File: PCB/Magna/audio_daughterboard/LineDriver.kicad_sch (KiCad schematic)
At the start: 27 parts, among them J101 PSG01550, Q101 NMOS, Q102 NMOS, U101 NE5532

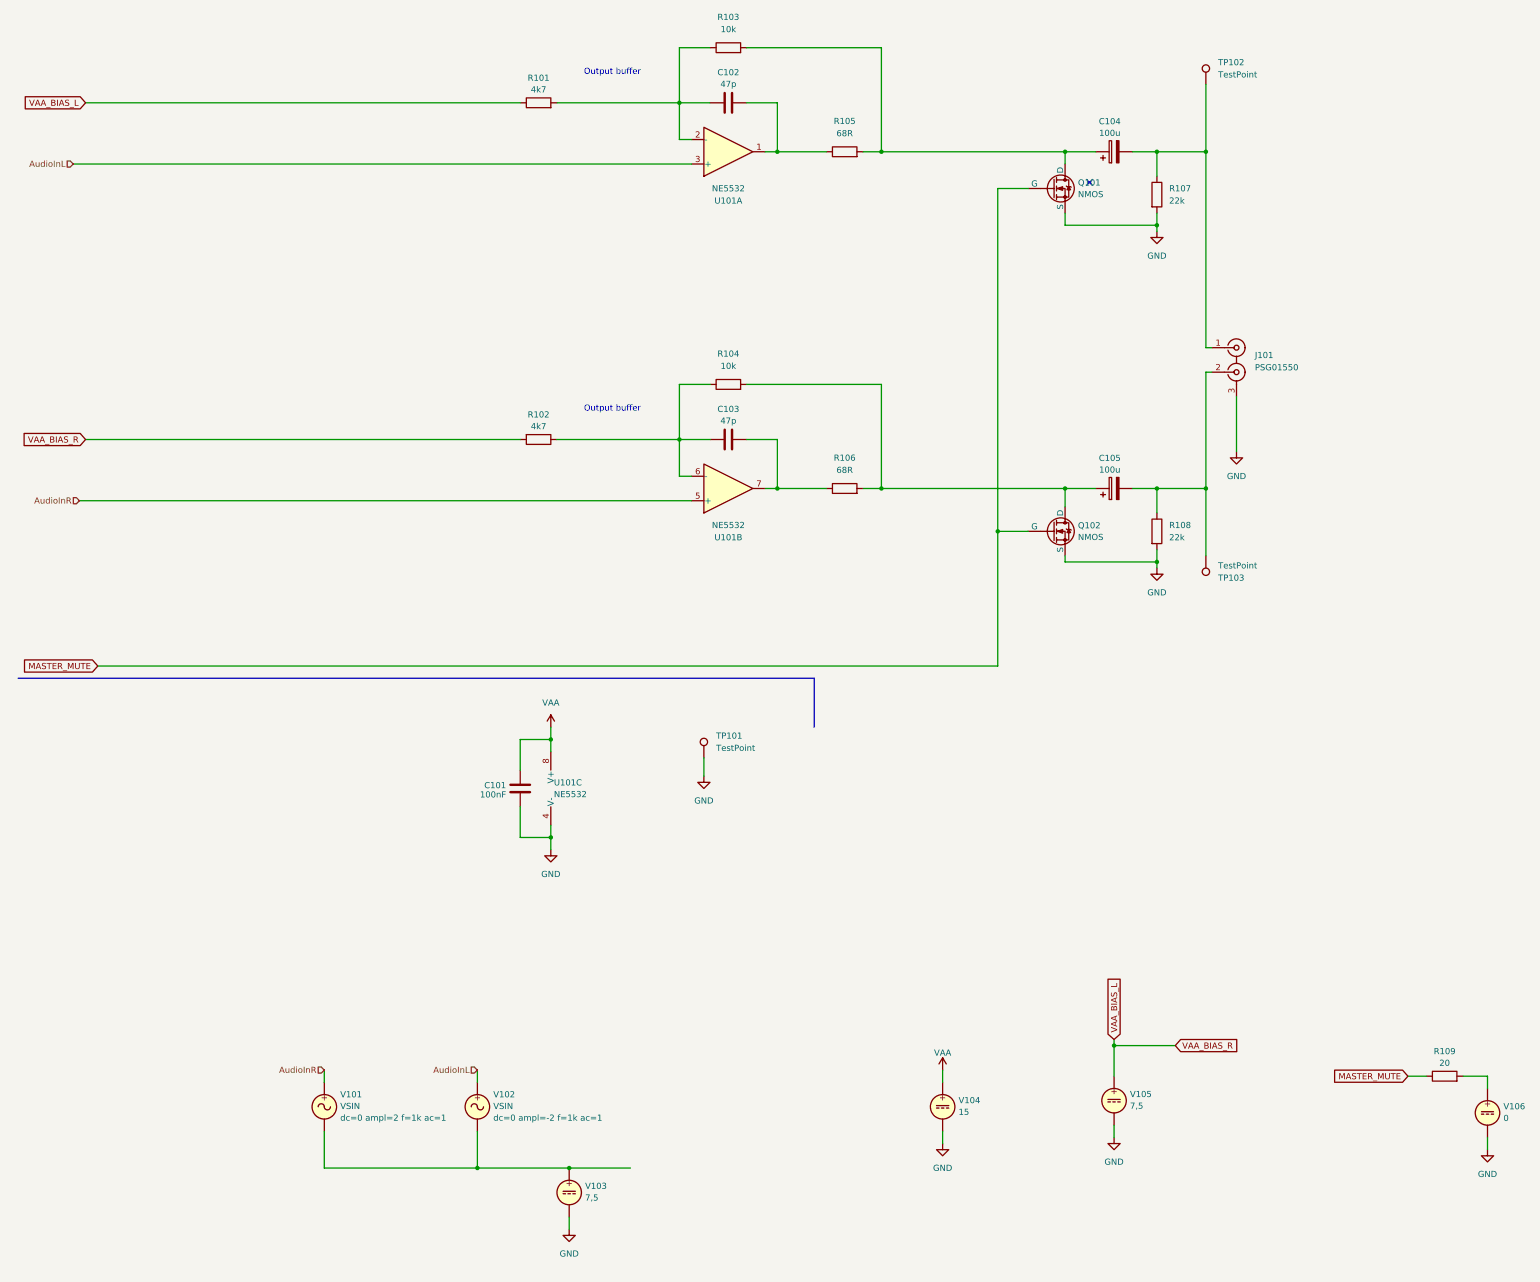
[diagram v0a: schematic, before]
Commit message: "Finalize" Audio daugherboard
Finished DAC output filter
Fixed the whole damn MCU subschematic
Fixed Linedriver schematic
Added component footprints and LCSC numbers
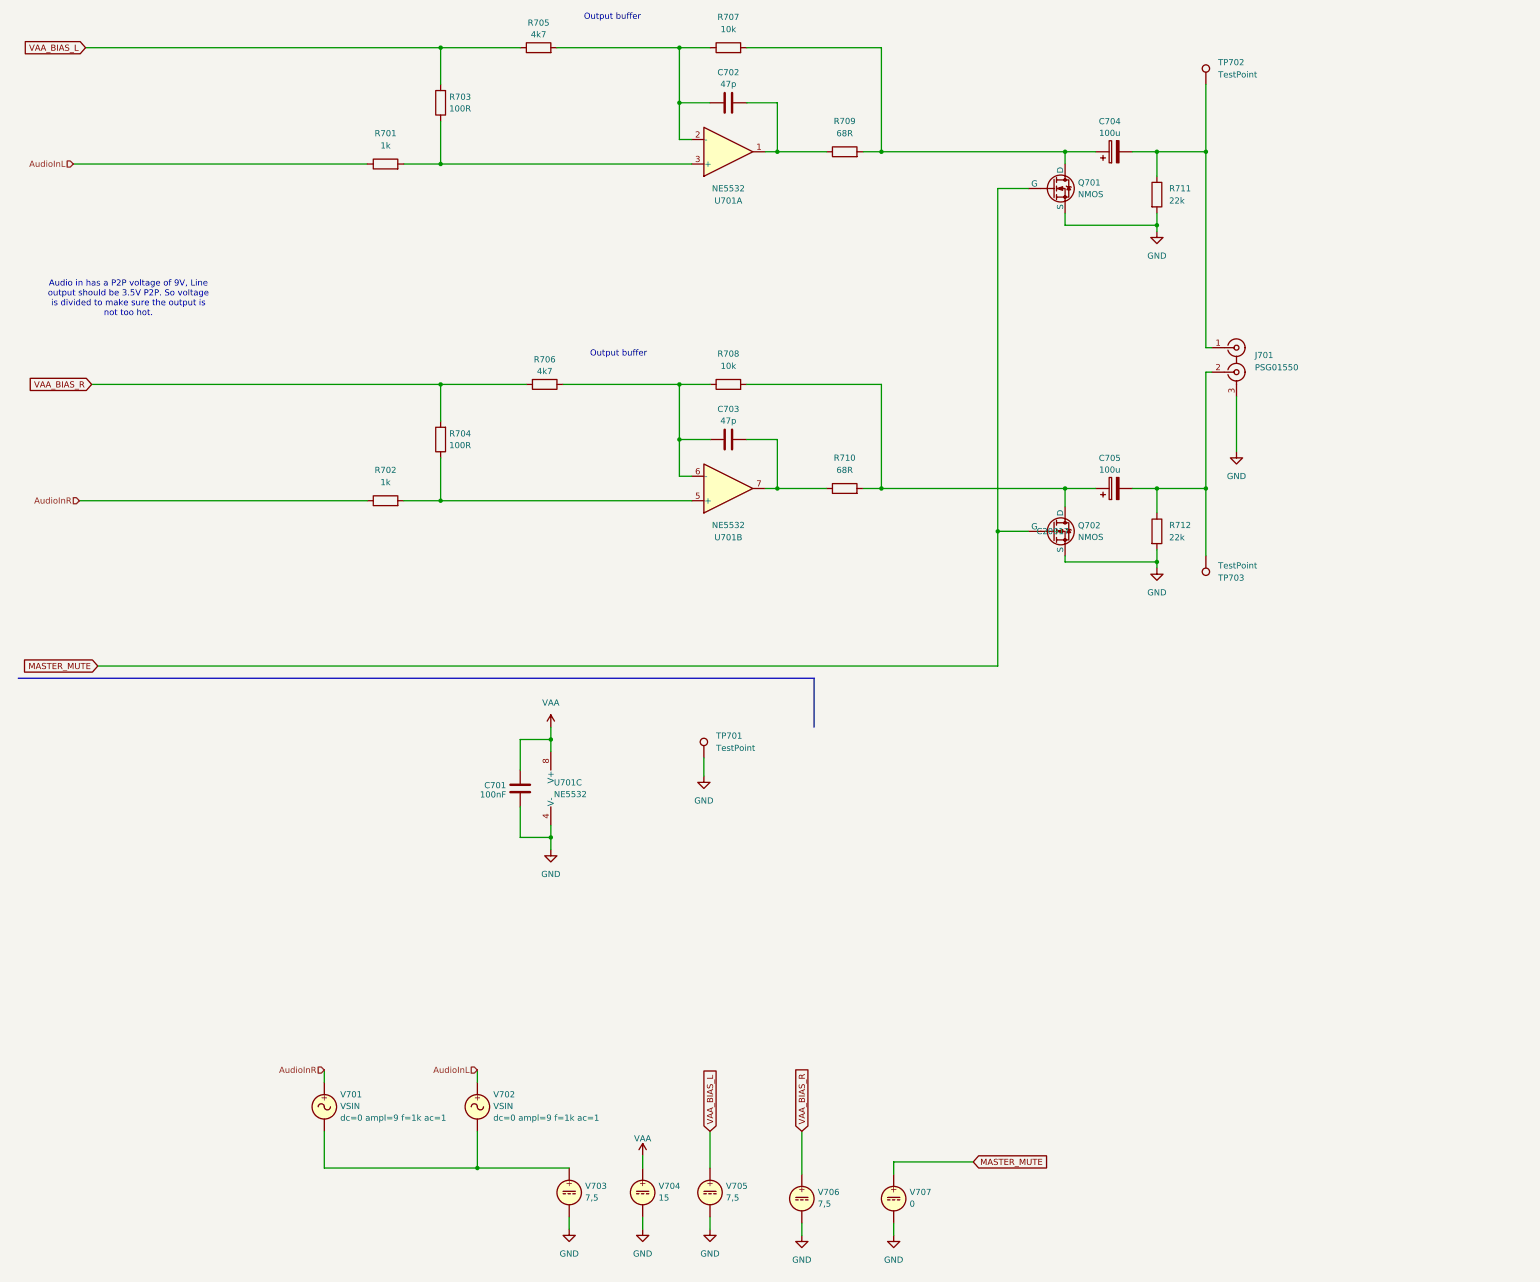
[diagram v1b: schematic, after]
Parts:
- removed C105: 100u, Capacitor_SMD:CP_Elec_6.3x5.8, symbol Device:C_Polarized
- removed R109: 20, Resistor_SMD:R_0805_2012Metric_Pad1.20x1.40mm_HandSolder, symbol Device:R
- added C705: 100u, Capacitor_SMD:CP_Elec_6.3x5.8, symbol Device:C_Polarized
- added R701, R702: 1k, Resistor_SMD:R_0603_1608Metric, symbol Device:R
- added R703, R704: 100R, Resistor_SMD:R_0603_1608Metric, symbol Device:R
- added V706: 7,5, symbol Simulation_SPICE:VDC
- C701: renamed from C101; now left out of the parts list
- C702: renamed from C102; now left out of the parts list
- C703: renamed from C103; now left out of the parts list
- C704: renamed from C104; now left out of the parts list
- J701: renamed from J101; now left out of the parts list
- Q701: renamed from Q101; footprint (none) -> Package_TO_SOT_SMD:SOT-23-3; LCSC (none) -> C20917; now left out of the parts list
- Q702: renamed from Q102; footprint (none) -> Package_TO_SOT_SMD:SOT-23-3; LCSC (none) -> C20917; now left out of the parts list
- R705: renamed from R101; footprint Resistor_SMD:R_0805_2012Metric_Pad1.20x1.40mm_HandSolder -> Resistor_SMD:R_0603_1608Metric; LCSC (none) -> C2989582; now left out of the parts list
- R706: renamed from R102; footprint Resistor_SMD:R_0805_2012Metric_Pad1.20x1.40mm_HandSolder -> Resistor_SMD:R_0603_1608Metric; LCSC (none) -> C2989582; now left out of the parts list
- R707: renamed from R103; footprint Resistor_SMD:R_0805_2012Metric_Pad1.20x1.40mm_HandSolder -> Resistor_SMD:R_0603_1608Metric; LCSC (none) -> C95204; now left out of the parts list
- R708: renamed from R104; footprint Resistor_SMD:R_0805_2012Metric_Pad1.20x1.40mm_HandSolder -> Resistor_SMD:R_0603_1608Metric; LCSC (none) -> C95204; now left out of the parts list
- R709: renamed from R105; footprint Resistor_SMD:R_0805_2012Metric_Pad1.20x1.40mm_HandSolder -> Resistor_SMD:R_0603_1608Metric; LCSC C865616 -> C351632; now left out of the parts list
- R710: renamed from R106; footprint Resistor_SMD:R_0805_2012Metric_Pad1.20x1.40mm_HandSolder -> Resistor_SMD:R_0603_1608Metric; LCSC C865616 -> C351632; now left out of the parts list
- R711: renamed from R107; footprint Resistor_SMD:R_0805_2012Metric_Pad1.20x1.40mm_HandSolder -> Resistor_SMD:R_0603_1608Metric; LCSC C479095 -> C335085; now left out of the parts list
- R712: renamed from R108; footprint Resistor_SMD:R_0805_2012Metric_Pad1.20x1.40mm_HandSolder -> Resistor_SMD:R_0603_1608Metric; LCSC C479095 -> C335085; now left out of the parts list
- TP701: renamed from TP101; now left out of the parts list
- TP702: renamed from TP102; now left out of the parts list
- TP703: renamed from TP103; now left out of the parts list
- U701: renamed from U101; now left out of the parts list
- V701: renamed from V101; now left out of the parts list
- V702: renamed from V102; now left out of the parts list
- V703: renamed from V103; now left out of the parts list
- V704: renamed from V104; now left out of the parts list
- V705: renamed from V105; now left out of the parts list
- V707: renamed from V106; now left out of the parts list
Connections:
- net AudioInL: now also R701.1; no longer U701.3 (+)
- net AudioInR: now also R702.1; no longer U701.5 (+)
- net GND: now also V706.2
- net MASTER_MUTE: now also V707.1
- net VAA_BIAS_L: now also R703.2; no longer R706.2
- net at J701.2 (IN2), R712.1, TP703.1: now also C705.2
- net at Q702.1 (D), R708.2, R710.2: now also C705.1
- new net: R702.2, R704.1, U701.5 (+)
- new net: R701.2, R703.1, U701.3 (+)
- new net VAA_BIAS_R: R704.2, R706.2, V706.1
- no-connect marks 1 -> 0
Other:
- note added: "Audio in has a P2P voltage of 9V, Line output should be 3.5V P2P. So voltage is divided to make sure the output is not too hot."
- moved on the sheet: R705, R706, V704, V705, V707

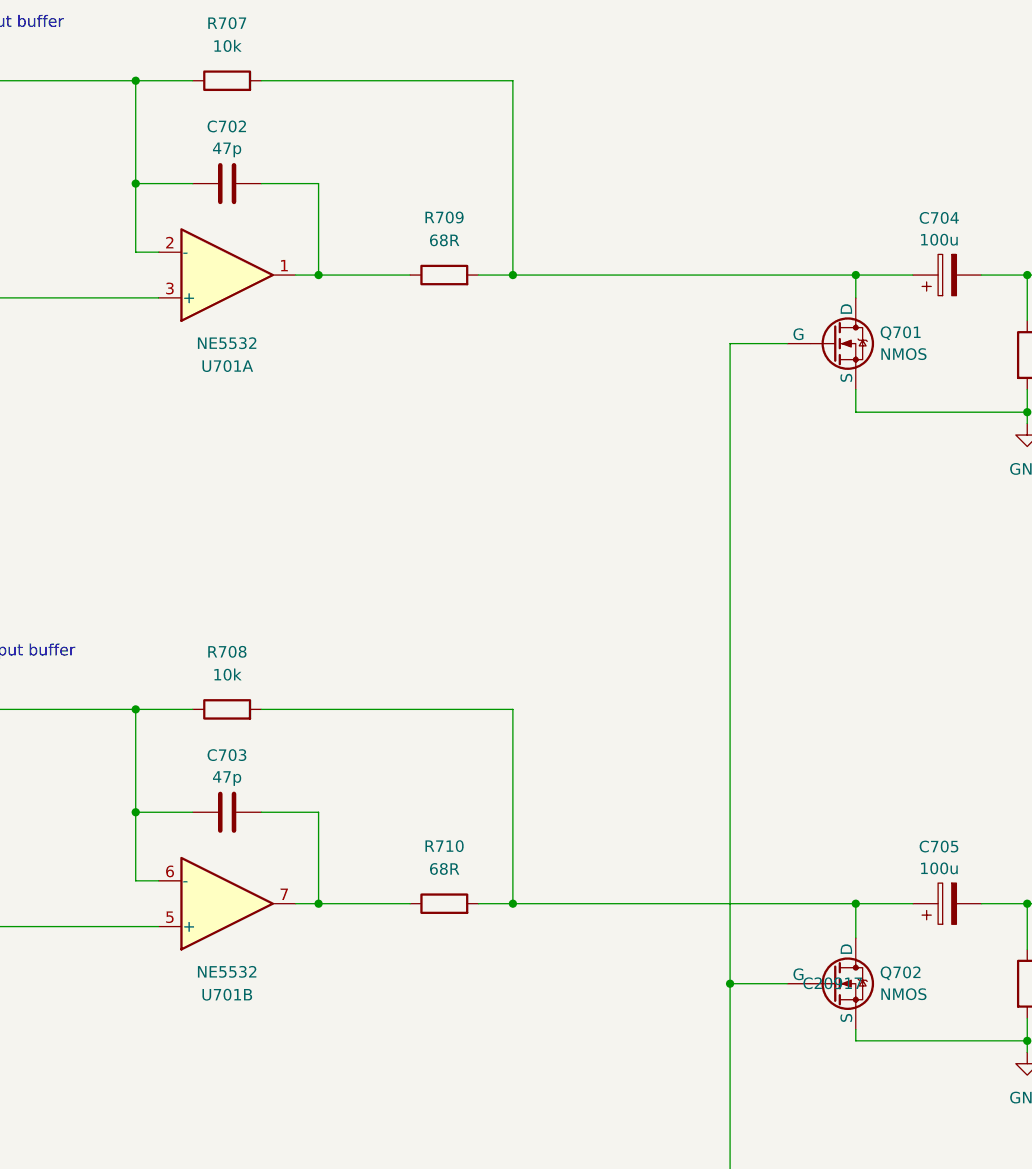
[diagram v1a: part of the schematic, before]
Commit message: Do most of the component placement for audio board
Just a general layout, things will probably change
as the routing begins.
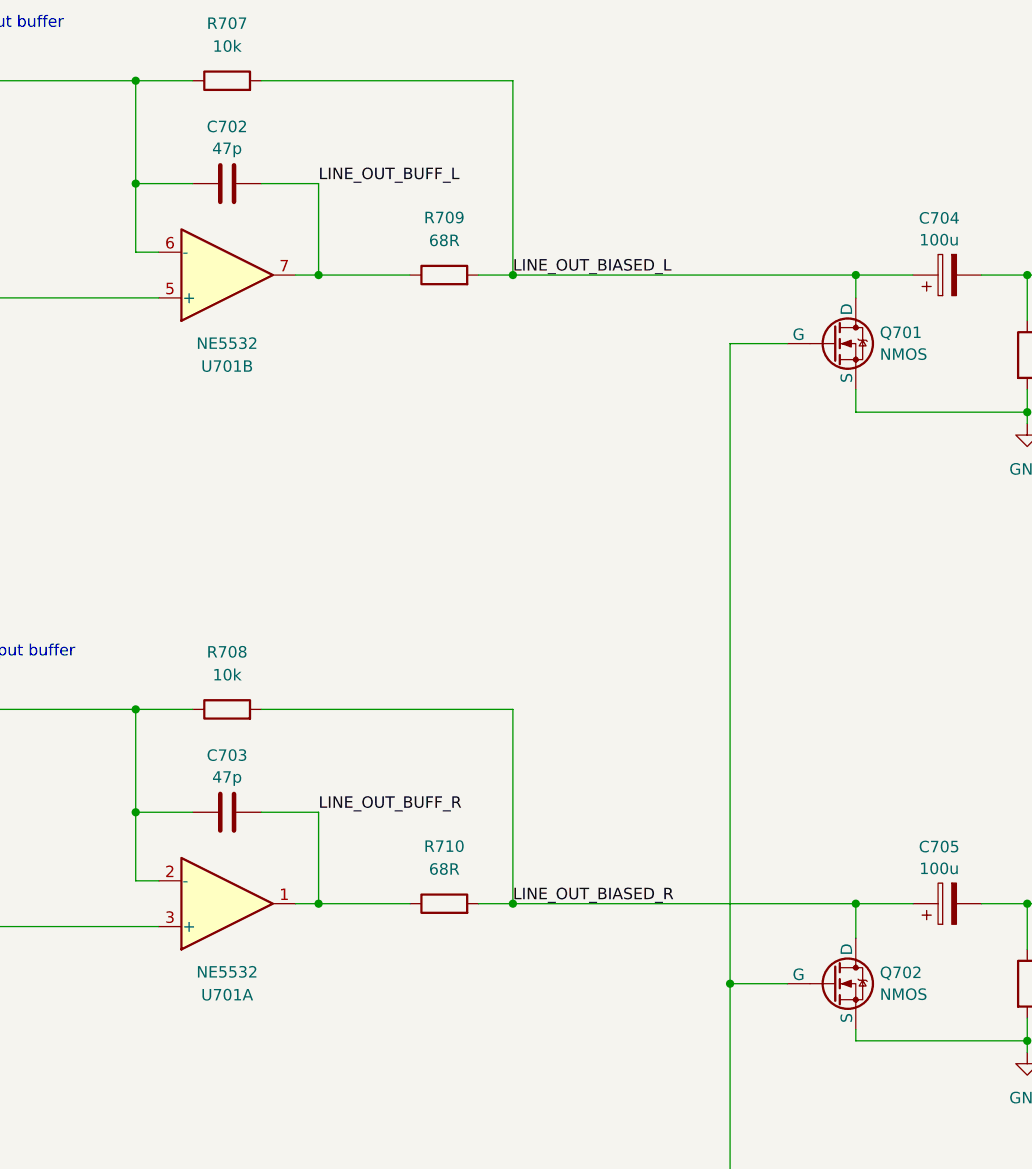
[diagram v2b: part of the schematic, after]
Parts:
- C701: footprint Capacitor_SMD:C_0805_2012Metric_Pad1.18x1.45mm_HandSolder -> Capacitor_SMD:C_0603_1608Metric; LCSC C49678 -> C14663
- C702, C703: footprint Capacitor_SMD:C_0805_2012Metric_Pad1.18x1.45mm_HandSolder -> Capacitor_SMD:C_0603_1608Metric; LCSC C14857 -> C1671
- C704, C705: footprint Capacitor_SMD:CP_Elec_6.3x5.8 -> Capacitor_SMD:CP_Elec_6.3x7.7; LCSC C2166157 -> C251007
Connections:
- net LINE_OUT_BUFF_R: now reaches C703.2, R710.1
- net LINE_OUT_BUFF_R: now also U701.1; no longer U701.7
- net LINE_OUT_BIASED_R: now reaches C705.1, Q702.1 (D), R708.2, R710.2
- net at R702.2, R704.1: now also U701.3 (+); no longer U701.5 (+)
- net at C703.1, R706.1, R708.1: now also U701.2 (-); no longer U701.6 (-)
- net LINE_OUT_BIASED_L: now reaches C704.1, Q701.1 (D), R707.2, R709.2
- net LINE_OUT_BUFF_L: now reaches C702.2, R709.1
- net LINE_OUT_BUFF_L: now also U701.7; no longer U701.1
- net at C702.1, R705.2, R707.1: now also U701.6 (-); no longer U701.2 (-)
- net at R701.2, R703.1: now also U701.5 (+); no longer U701.3 (+)
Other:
- moved on the sheet: U701A, U701B
